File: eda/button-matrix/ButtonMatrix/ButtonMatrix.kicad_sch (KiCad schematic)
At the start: 18 parts, among them SW1 SW_Omron_B3FS, SW10 SW_Omron_B3FS, SW11 SW_Omron_B3FS, SW12 SW_Omron_B3FS, SW13 SW_Omron_B3FS, SW14 SW_Omron_B3FS, SW15 SW_Omron_B3FS, SW16 SW_Omron_B3FS, SW2 SW_Omron_B3FS, SW3 SW_Omron_B3FS, SW4 SW_Omron_B3FS, SW5 SW_Omron_B3FS, SW6 SW_Omron_B3FS, SW7 SW_Omron_B3FS, SW8 SW_Omron_B3FS, SW9 SW_Omron_B3FS

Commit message: - Updated the pcb for the new 4x4 button matrix - Added support imgui and desktop support
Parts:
- removed D1: LED_RGBA, LED_THT:LED_D5.0mm-4_RGB_Wide_Pins, symbol Device:LED_RGBA
- removed D3: LED_RGBA, LED_THT:LED_D5.0mm-4_RGB, symbol Device:LED_RGBA
- added D1, D10, D11, D12, D13, D14, D15, D16, D2, D3, D4, D5, D6, D7, D8, D9: 1N4148, Diode_THT:D_DO-35_SOD27_P7.62mm_Horizontal, symbol Diode:1N4148
- added D17: LED_RGBA, LED_THT:LED_D5.0mm-4_RGB, symbol Device:LED_RGBA
- added D18: LED_RGBA, LED_THT:LED_D5.0mm-4_RGB_Wide_Pins, symbol Device:LED_RGBA
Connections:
- net SW_ROW4: now reaches SW13.1
- net SW_ROW4: now also SW14.1, SW15.1, SW16.1
- net SW_ROW1: now reaches SW1.1
- net SW_ROW1: now also SW2.1, SW3.1, SW4.1
- net SW_ROW2: now reaches SW5.1
- net SW_ROW2: now also SW6.1, SW7.1, SW8.1
- net SW_ROW3: now reaches SW9.1
- net SW_ROW3: now also SW10.1, SW11.1, SW12.1
- new net: D11.2 (A), SW11.2
- new net: D1.2 (A), SW1.2
- new net: D16.2 (A), SW16.2
- new net: D15.2 (A), SW15.2
- new net: D12.2 (A), SW12.2
- new net: D14.2 (A), SW14.2
- new net: D13.2 (A), SW13.2
- new net: D9.2 (A), SW9.2
- new net: D7.2 (A), SW7.2
- new net: D2.2 (A), SW2.2
- new net: D4.2 (A), SW4.2
- new net: D8.2 (A), SW8.2
- new net: D3.2 (A), SW3.2
- new net: D10.2 (A), SW10.2
- new net: D6.2 (A), SW6.2
- new net: D5.2 (A), SW5.2
- new net SW_COL1: D1.1 (K), D13.1 (K), D5.1 (K), D9.1 (K)
- new net SW_COL2: D10.1 (K), D14.1 (K), D2.1 (K), D6.1 (K)
- new net SW_COL3: D11.1 (K), D15.1 (K), D3.1 (K), D7.1 (K)
- new net SW_COL4: D12.1 (K), D16.1 (K), D4.1 (K), D8.1 (K)
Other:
- moved on the sheet: SW1, SW10, SW11, SW12, SW13, SW14, SW15, SW16, SW2, SW3, SW4, SW5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

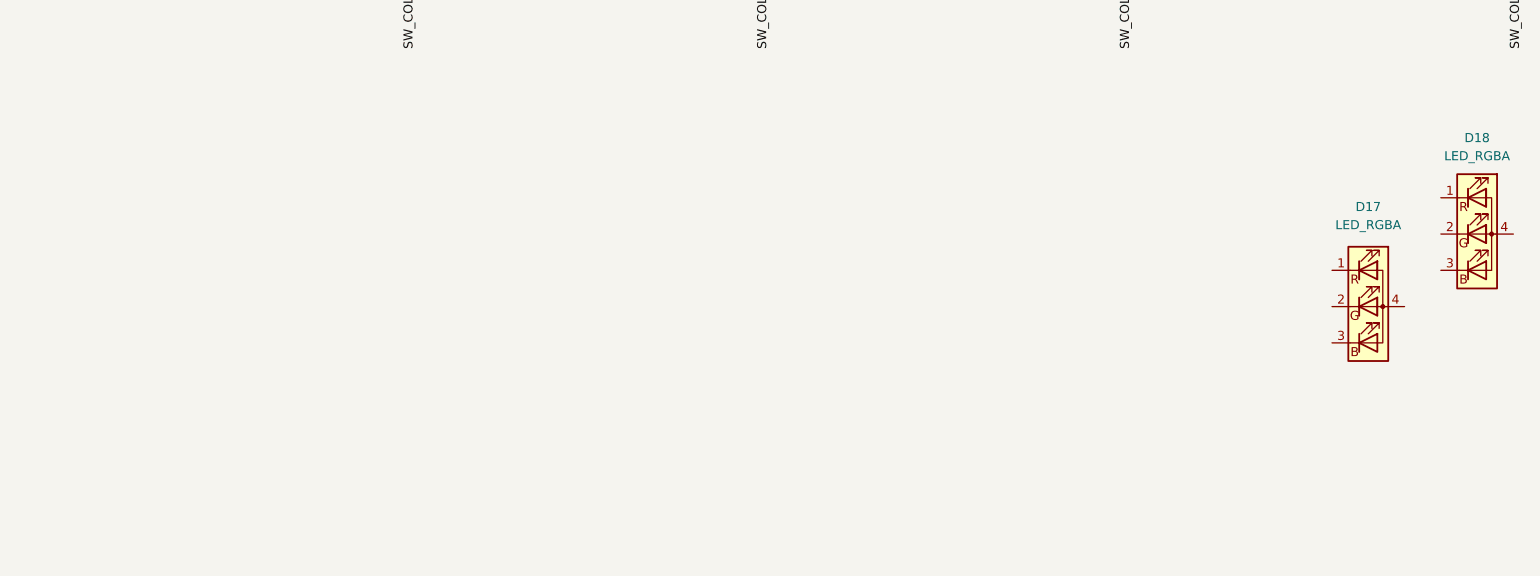
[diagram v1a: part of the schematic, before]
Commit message: - Added m2 mounting holes to the pcb
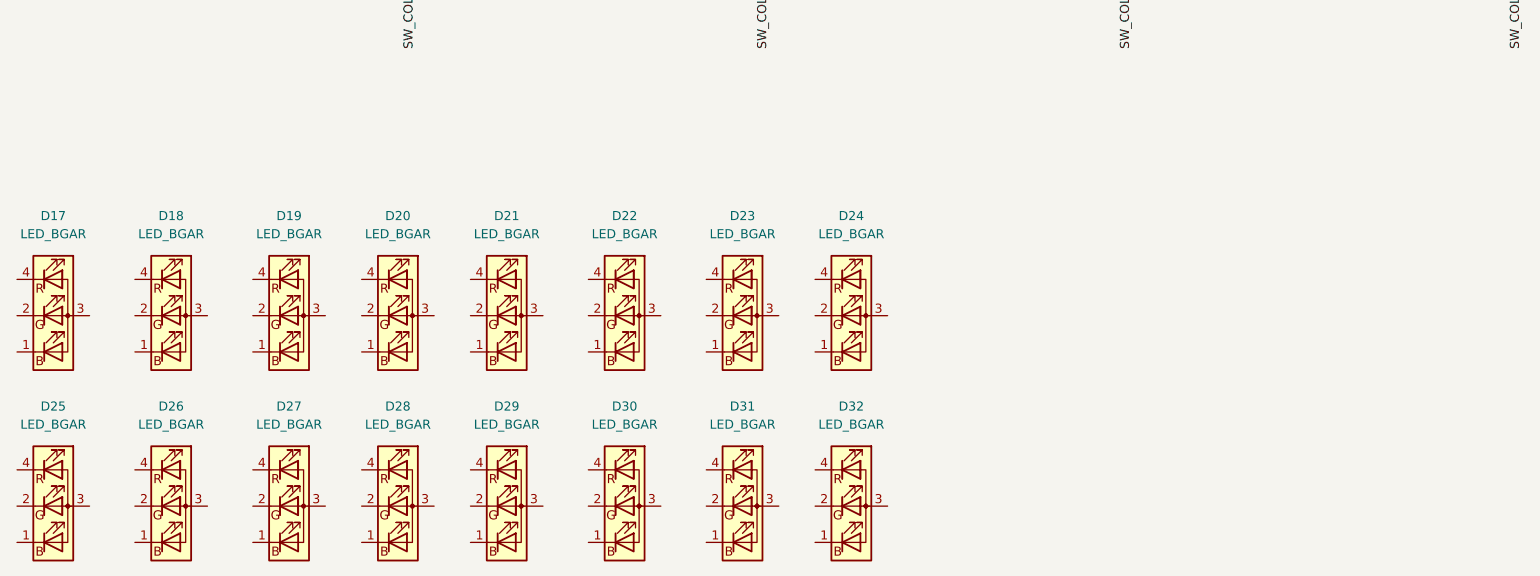
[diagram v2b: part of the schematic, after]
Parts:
- removed D17: LED_RGBA, LED_THT:LED_D5.0mm-4_RGB, symbol Device:LED_RGBA
- removed D18: LED_RGBA, LED_THT:LED_D5.0mm-4_RGB_Wide_Pins, symbol Device:LED_RGBA
- added D17, D18, D19, D20, D21, D22, D23, D24, D25, D26, D27, D28, D29, D30, D31, D32: LED_BGAR, LED_THT:LED_D5.0mm-4_RGB, symbol Device:LED_BGAR

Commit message: - Added headers and connected all diods
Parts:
- added J1, J2: Conn_01x12, Connector_PinHeader_2.54mm:PinHeader_1x11_P2.54mm_Vertical, symbol Connector_Generic:Conn_01x12
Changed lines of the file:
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@@
+	)
+	(symbol
+		(lib_id "Connector_Generic:Conn_01x12")
+		(at 215.9 140.97 0)
+		(unit 1)
+		(exclude_from_sim no)
+		(in_bom yes)
+		(on_board yes)
+		(dnp no)
+		(fields_autoplaced yes)
+		(property "Reference" "J2"
+			(at 218.44 140.9699 0)
+			(effects
+				(font
+					(size 1.27 1.27)
+				)
+				(justify left)
+			)
+		)
+		(property "Value" "Conn_01x12"
+			(at 218.44 143.5099 0)
+			(effects
+				(font
+					(size 1.27 1.27)
+				)
+				(justify left)
+			)
+		)
+		(property "Footprint" "Connector_PinHeader_2.54mm:PinHeader_1x11_P2.54mm_Vertical"
+			(at 215.9 140.97 0)
+			(effects
+				(font
+					(size 1.27 1.27)
+				)
+				(hide yes)
+			)
+		)
+		(property "Datasheet" "~"
+			(at 215.9 140.97 0)
+			(effects
+				(font
+					(size 1.27 1.27)
+				)
+				(hide yes)
+			)
+		)
+		(property "Description" "Generic connector, single row, 01x12, script generated (kicad-library-utils/schlib/autogen/connector/)"
+			(at 215.9 140.97 0)
+			(effects
+				(font
+					(size 1.27 1.27)
+				)
+				(hide yes)
+			)
+		)
+		(pin "3"
+		)
+		(pin "4"
+		)
+		(pin "5"
+		)
+		(pin "6"
+		)
+		(pin "7"
+		)
+		(pin "1"
+		)
+		(pin "2"
+		)
+		(pin "8"
+		)
+		(pin "9"
+		)
+		(pin "10"
+		)
+		(pin "11"
+		)
+		(pin "12"
+		)
+		(instances
+			(project "ButtonMatrix"
+				(path "/a9cc6e02-ad1b-41d7-8cd8-8cf0c6fe637e"
+					(reference "J2")
+					(unit 1)
+				)
+			)
+		)
 	)
 	(symbol
@@
 					(unit 1)
 				)
+			)
+		)
+	)
+	(symbol
+		(lib_id "Connector_Generic:Conn_01x12")
+		(at 184.15 139.7 0)
+		(unit 1)
+		(exclude_from_sim no)
+		(in_bom yes)
+		(on_board yes)
+		(dnp no)
+		(fields_autoplaced yes)
+		(property "Reference" "J1"
+			(at 186.69 139.6999 0)
+			(effects
+				(font
+					(size 1.27 1.27)
+				)
+				(justify left)
+			)
+		)
+		(property "Value" "Conn_01x12"
+			(at 186.69 142.2399 0)
+			(effects
+				(font
+					(size 1.27 1.27)
+				)
+				(justify left)
+			)
+		)
+		(property "Footprint" "Connector_PinHeader_2.54mm:PinHeader_1x11_P2.54mm_Vertical"
+			(at 184.15 139.7 0)
+			(effects
+				(font
+					(size 1.27 1.27)
+				)
+				(hide yes)
+			)
+		)
+		(property "Datasheet" "~"
+			(at 184.15 139.7 0)
+			(effects
+				(font
+					(size 1.27 1.27)
+				)
+				(hide yes)
+			)
+		)
+		(property "Description" "Generic connector, single row, 01x12, script generated (kicad-library-utils/schlib/autogen/connector/)"
+			(at 184.15 139.7 0)
+			(effects
+				(font
+					(size 1.27 1.27)
+				)
+				(hide yes)
+			)
+		)
+		(pin "3"
+		)
+		(pin "4"
+		)
+		(pin "5"
+		)
+		(pin "6"
+		)
+		(pin "7"
+		)
+		(pin "1"
+		)
+		(pin "2"
+		)
+		(pin "8"
+		)
+		(pin "9"
+		)
+		(pin "10"
+		)
+		(pin "11"
+		)
+		(pin "12"
+		)
+		(instances
+			(project ""
+				(path "/a9cc6e02-ad1b-41d7-8cd8-8cf0c6fe637e"
+					(reference "J1")
+					(unit 1)
+				)

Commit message: - Updated PCB more
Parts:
- J1, J2: footprint Connector_PinHeader_2.54mm:PinHeader_1x11_P2.54mm_Vertical -> Connector_PinHeader_2.54mm:PinHeader_1x12_P2.54mm_Vertical
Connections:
- net SW_COL1: now also J1.5 (Pin_5)
- net SW_COL2: now also J1.6 (Pin_6)
- net SW_COL3: now also J1.7 (Pin_7)
- net SW_COL4: now also J1.8 (Pin_8)
- net SW_ROW1: now also J1.1 (Pin_1)
- net SW_ROW2: now also J1.2 (Pin_2)
- net SW_ROW3: now also J1.3 (Pin_3)
- net SW_ROW4: now also J1.4 (Pin_4)
- net LED_B2: now reaches D22.1 (BK)
- net LED_B2: now also D21.1 (BK), D23.1 (BK), D24.1 (BK), J2.6 (Pin_6)
- net LED_G2: now reaches D22.2 (GK)
- net LED_G2: now also D21.2 (GK), D23.2 (GK), D24.2 (GK), J2.5 (Pin_5)
- net LED_COL2: now reaches D22.3 (A)
- net LED_COL2: now also D18.3 (A), D26.3 (A), D30.3 (A), J1.10 (Pin_10)
- net LED_R2: now reaches D22.4 (RK)
- net LED_R2: now also D21.4 (RK), D23.4 (RK), D24.4 (RK), J2.4 (Pin_4)
- net LED_B3: now reaches D25.1 (BK)
- net LED_B3: now also D26.1 (BK), D27.1 (BK), D28.1 (BK), J2.9 (Pin_9)
- net LED_G3: now reaches D25.2 (GK)
- net LED_G3: now also D26.2 (GK), D27.2 (GK), D28.2 (GK), J2.8 (Pin_8)
- net LED_COL1: now reaches D25.3 (A)
- net LED_COL1: now also D17.3 (A), D21.3 (A), D29.3 (A), J1.9 (Pin_9)
- net LED_R3: now reaches D25.4 (RK)
- net LED_R3: now also D26.4 (RK), D27.4 (RK), D28.4 (RK), J2.7 (Pin_7)
- net LED_COL4: now reaches D24.3 (A)
- net LED_COL4: now also D20.3 (A), D28.3 (A), D32.3 (A), J1.12 (Pin_12)
- net LED_COL3: now reaches D27.3 (A)
- net LED_COL3: now also D19.3 (A), D23.3 (A), D31.3 (A), J1.11 (Pin_11)
- net LED_B1: now reaches D17.1 (BK)
- net LED_B1: now also D18.1 (BK), D19.1 (BK), D20.1 (BK), J2.3 (Pin_3)
- net LED_G1: now reaches D17.2 (GK)
- net LED_G1: now also D18.2 (GK), D19.2 (GK), D20.2 (GK), J2.2 (Pin_2)
- net LED_R1: now reaches D17.4 (RK)
- net LED_R1: now also D18.4 (RK), D19.4 (RK), D20.4 (RK), J2.1 (Pin_1)
- net LED_R4: now reaches J2.10 (Pin_10)
- net LED_R4: now also D29.4 (RK), D30.4 (RK), D31.4 (RK), D32.4 (RK)
- net LED_G4: now reaches J2.11 (Pin_11)
- net LED_G4: now also D29.2 (GK), D30.2 (GK), D31.2 (GK), D32.2 (GK)
- net LED_B4: now reaches J2.12 (Pin_12)
- net LED_B4: now also D29.1 (BK), D30.1 (BK), D31.1 (BK), D32.1 (BK)
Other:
- moved on the sheet: D1, D10, D11, D12, D13, D14, D15, D16, D17, D18, D19, D2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

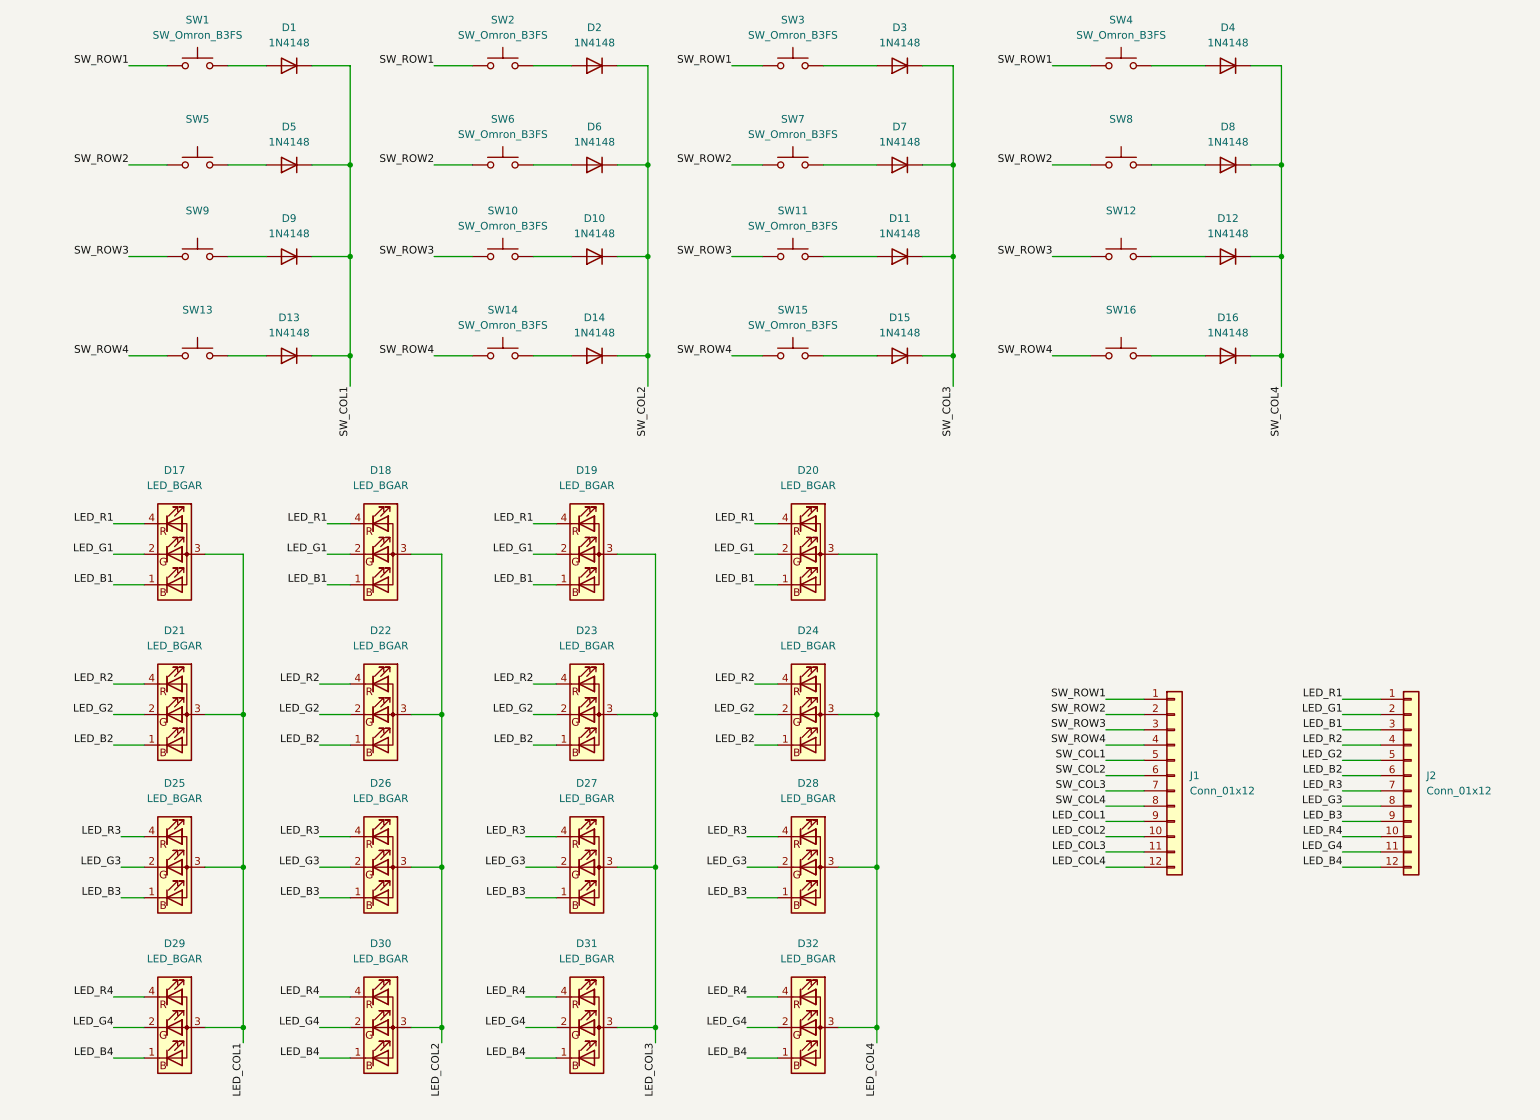
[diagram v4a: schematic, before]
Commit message: - Fixed issue in my lumisquare button footrprint - Redesign teh button fill areas to better alingn witht he button mask
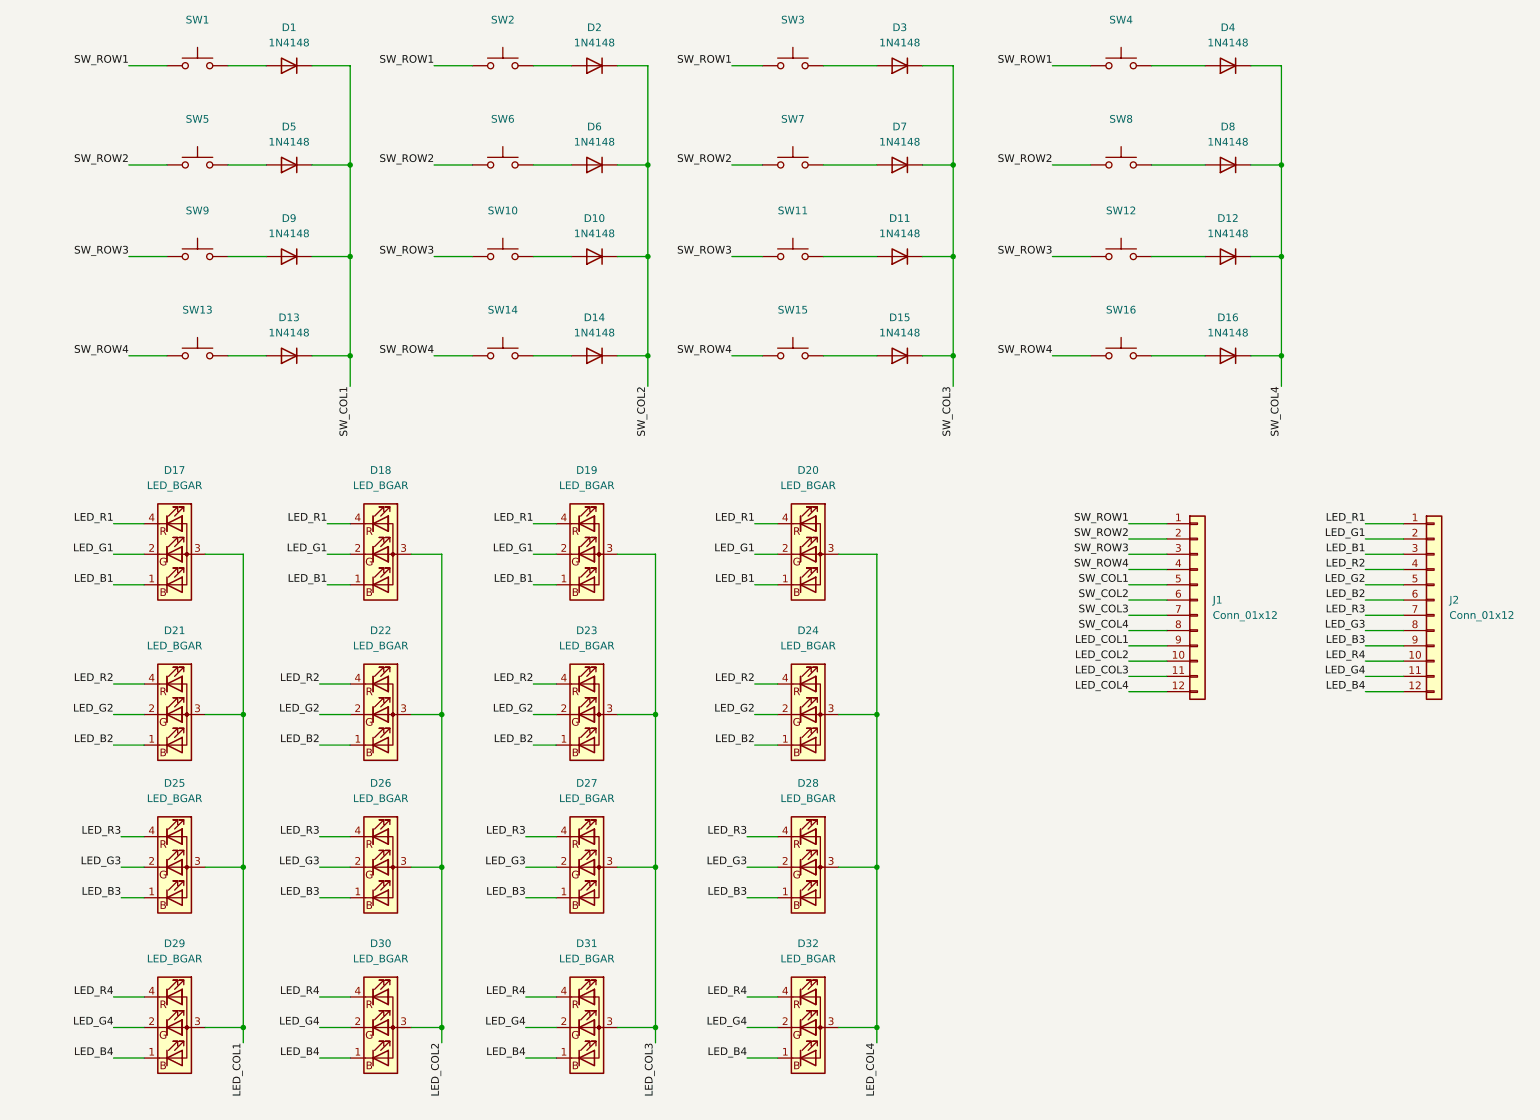
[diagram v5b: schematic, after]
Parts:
- SW1, SW10, SW11, SW12, SW13, SW14, SW15, SW16, SW2, SW3, SW4, SW5, SW6, SW7, SW8, SW9: value SW_Omron_B3FS -> (none)
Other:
- moved on the sheet: J1, J2
